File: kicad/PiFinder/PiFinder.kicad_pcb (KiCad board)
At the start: 2 copper layers, 87.9 x 57.7 mm, 24 parts, among them J1 Raspberry_Pi_2_3, J2 display, J3 IMU, SW0 SW_Push_Dual, SW1 SW_Push_Dual, SW2 SW_Push_Dual, SW3 SW_Push_Dual, SW4 SW_Push_Dual, SW5 SW_Push_Dual, SW6 SW_Push_Dual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

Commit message: Working capture/solver
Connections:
- J2 pad 3: unconnected-(J2-Pad3) -> DISP_DIN
- J2 pad 4: DISP_DIN -> DISP_CLK
- J2 pad 5: DISP_CLK -> DISP_CS
- J2 pad 6: DISP_CS -> DISP_DC
- J2 pad 7: DISP_DC -> DISP_RST
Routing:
- net DISP_RST: track 71.7 -> 74.6 mm
- net DISP_CS: track 72.1 -> 74.7 mm
- net DISP_DIN: track 71.8 -> 72.9 mm
- net DISP_DC: track 72.8 -> 73.9 mm
- net DISP_CLK: track 65.5 -> 66.6 mm

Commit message: Add power, fix imu connection to main PCB
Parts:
- added J4: Pwr, Connector_PinHeader_2.00mm:PinHeader_1x02_P2.00mm_Horizontal, F.Cu at (102.4, 114.8)
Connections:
- J1 pad 2: unconnected-(J1-Pad2) -> +5V
- J1 pad 4: unconnected-(J1-Pad4) -> +5V
- J3 pad 4: I2C_SDA -> I2C_SCL
- J3 pad 5: I2C_SCL -> I2C_SDA
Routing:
- net +5V: track 0.00 -> 72.5 mm
- net I2C_SCL: track 63.9 -> 64.9 mm, vias 0 -> 1
- net I2C_SDA: track 66.6 -> 65.5 mm

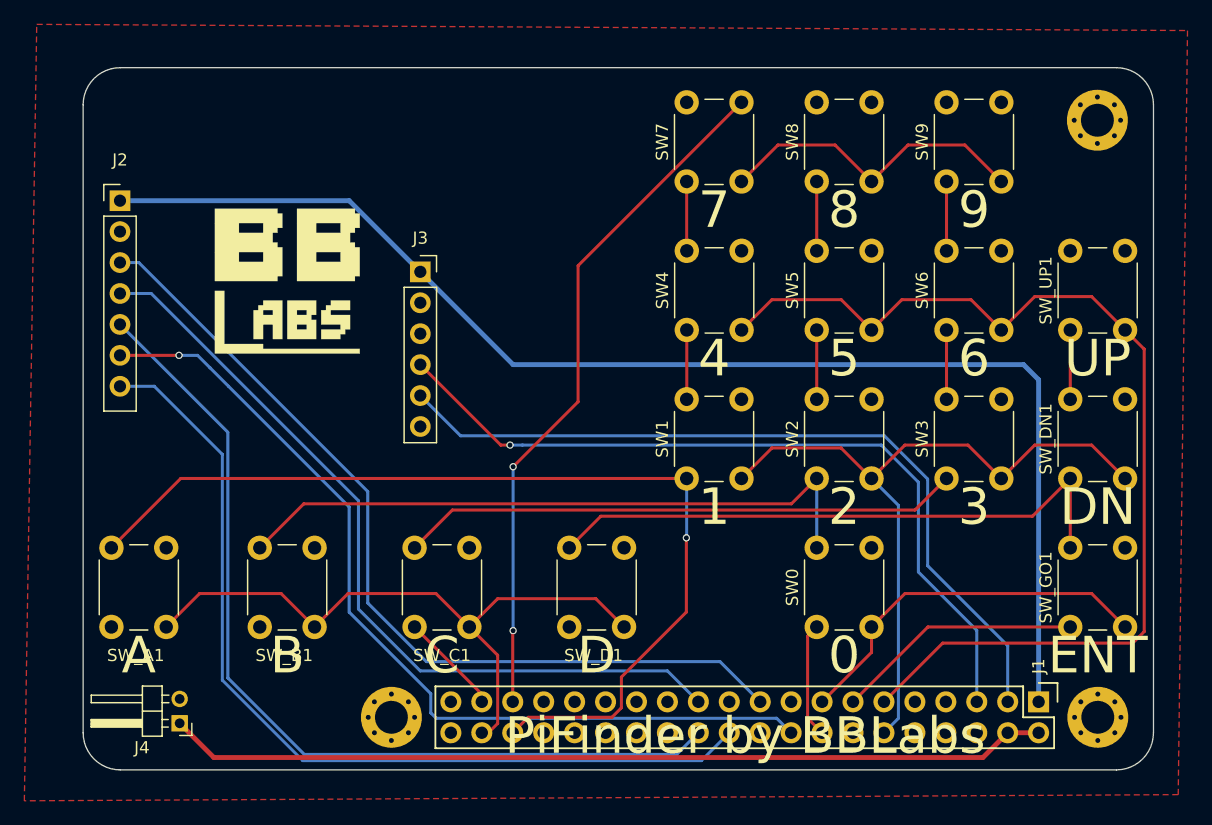
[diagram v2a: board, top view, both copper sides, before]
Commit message: New PCB with backlight
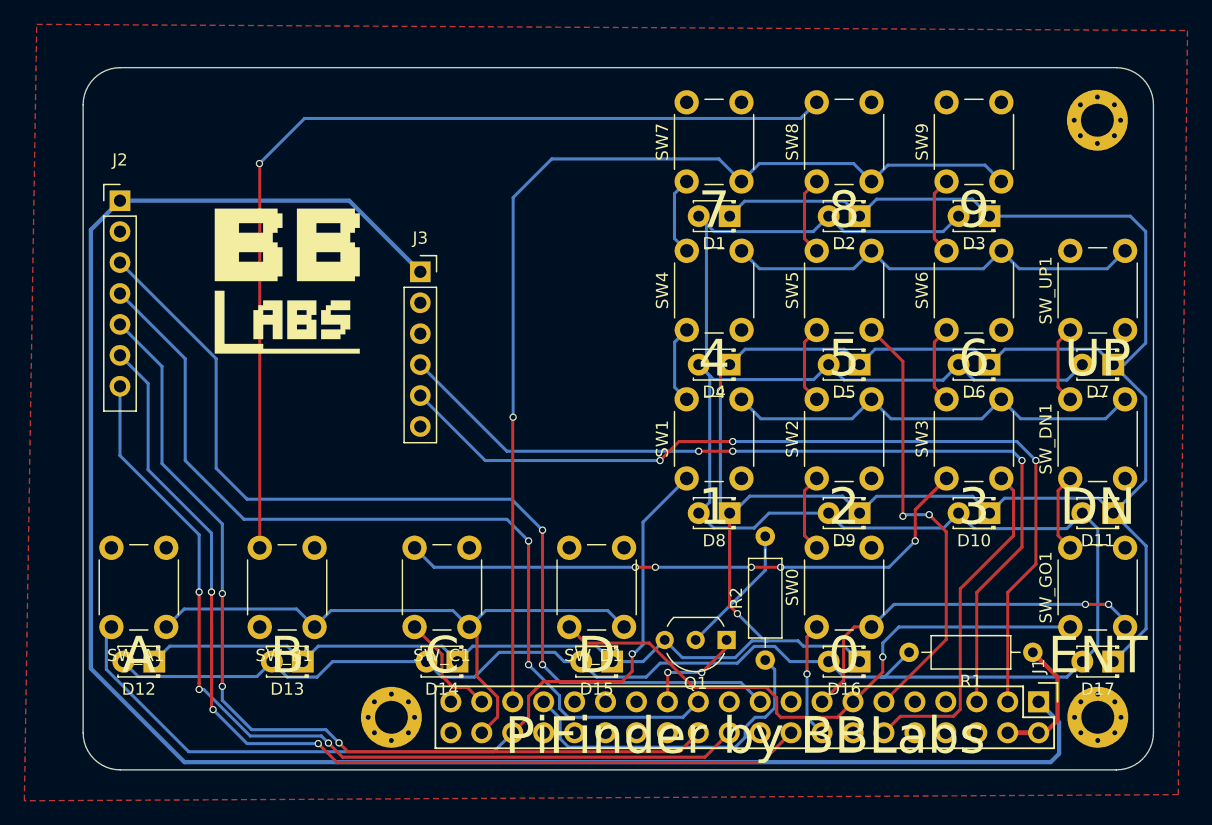
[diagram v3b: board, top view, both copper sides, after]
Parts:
- removed J4: Pwr, Connector_PinHeader_2.00mm:PinHeader_1x02_P2.00mm_Horizontal
- added D1: LED, LED_THT:LED_D1.8mm_W3.3mm_H2.4mm, F.Cu at (147.6, 73.2)
- added D10: LED, LED_THT:LED_D1.8mm_W3.3mm_H2.4mm, F.Cu at (168.9, 97.5)
- added D11: LED, LED_THT:LED_D1.8mm_W3.3mm_H2.4mm, F.Cu at (179.1, 97.5)
- added D12: LED, LED_THT:LED_D1.8mm_W3.3mm_H2.4mm, F.Cu at (100.3, 109.7)
- added D13: LED, LED_THT:LED_D1.8mm_W3.3mm_H2.4mm, F.Cu at (112.5, 109.7)
- added D14: LED, LED_THT:LED_D1.8mm_W3.3mm_H2.4mm, F.Cu at (125.2, 109.7)
- added D15: LED, LED_THT:LED_D1.8mm_W3.3mm_H2.4mm, F.Cu at (137.9, 109.7)
- added D16: LED, LED_THT:LED_D1.8mm_W3.3mm_H2.4mm, F.Cu at (158.2, 109.7)
- added D17: LED, LED_THT:LED_D1.8mm_W3.3mm_H2.4mm, F.Cu at (179.1, 109.7)
- added D2: LED, LED_THT:LED_D1.8mm_W3.3mm_H2.4mm, F.Cu at (158.2, 73.2)
- added D3: LED, LED_THT:LED_D1.8mm_W3.3mm_H2.4mm, F.Cu at (168.9, 73.2)
- added D4: LED, LED_THT:LED_D1.8mm_W3.3mm_H2.4mm, F.Cu at (147.6, 85.3)
- added D5: LED, LED_THT:LED_D1.8mm_W3.3mm_H2.4mm, F.Cu at (158.2, 85.3)
- added D6: LED, LED_THT:LED_D1.8mm_W3.3mm_H2.4mm, F.Cu at (168.9, 85.3)
- added D7: LED, LED_THT:LED_D1.8mm_W3.3mm_H2.4mm, F.Cu at (179.1, 85.3)
- added D8: LED, LED_THT:LED_D1.8mm_W3.3mm_H2.4mm, F.Cu at (147.6, 97.5)
- added D9: LED, LED_THT:LED_D1.8mm_W3.3mm_H2.4mm, F.Cu at (158.2, 97.5)
- added Q1: Q_NPN_EBC, Package_TO_SOT_THT:TO-92_Inline_Wide, F.Cu at (147.3, 108.0)
- added R1: 22, Resistor_THT:R_Axial_DIN0207_L6.3mm_D2.5mm_P10.16mm_Horizontal, F.Cu at (172.5, 109.0)
- added R2: 330, Resistor_THT:R_Axial_DIN0207_L6.3mm_D2.5mm_P10.16mm_Horizontal, F.Cu at (150.5, 109.6)
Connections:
- J1 pad 33: unconnected-(J1-Pad33) -> LED_PWM
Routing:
- net LED_C: track 0.00 -> 236.1 mm, vias 0 -> 2
- net LED_A: track 0.00 -> 220.3 mm
- net +5V: track 72.5 -> 13.5 mm
- net +3.3V: track 108.0 -> 154.4 mm
- net COL1: track 74.7 -> 108.5 mm, vias 0 -> 2
- net LED_PWM: track 0.00 -> 27.6 mm
- net ROW1: track 87.1 -> 71.8 mm, vias 0 -> 2
- net COL3: track 75.3 -> 62.5 mm, vias 0 -> 1
- net Net-(Q1-Pad2): track 0.00 -> 10.9 mm
- net I2C_SDA: track 65.5 -> 74.8 mm, vias 0 -> 3
- net I2C_SCL: track 64.9 -> 74.0 mm, vias 1 -> 3
- net GND: track 0.00 -> 8.73 mm, vias 0 -> 2
- net DISP_DC: track 73.9 -> 82.5 mm, vias 1 -> 3
- net COL0: track 91.8 -> 84.2 mm
- net DISP_CLK: track 66.6 -> 73.9 mm, vias 0 -> 2
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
